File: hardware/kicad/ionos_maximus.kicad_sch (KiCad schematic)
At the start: 45 parts, among them J1 CLH-115-F-D-DV, J2 NA(TC2030-NL), P200 TFC-120-02-F-D-A-K-TR, P201 TFC-120-02-F-D-A-K-TR, U1 LP5907MFX-3.3, U2 CAT24C32WI-GT3

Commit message: Docs from the twin: BRD4265B has no BOARD_ID SDA/SCL pull-ups (Pi 1k8 serve I2C1); P200-37 is USB_VBUS, not 5V
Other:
- note added: "pull-ups: 1k8 on the Pi, none on the radio board (only WP)."
- note removed: "pull-ups 1k8 on the Pi, 10k on the radio board."
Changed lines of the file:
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@@
 		)
 	)
-	(text "pull-ups 1k8 on the Pi, 10k on the radio board."
+	(text "pull-ups: 1k8 on the Pi, none on the radio board (only WP)."
 		(exclude_from_sim no)
 		(at 284.48 121.92 0)
@@
 			)
 		)
-		(property "Description" "P200-37 5 V option, not fitted"
+		(property "Description" "P200-37 = USB_VBUS on BRD4265B (5V is P200-35), not fitted"
 			(at 210.82 182.88 0)
 			(hide yes)

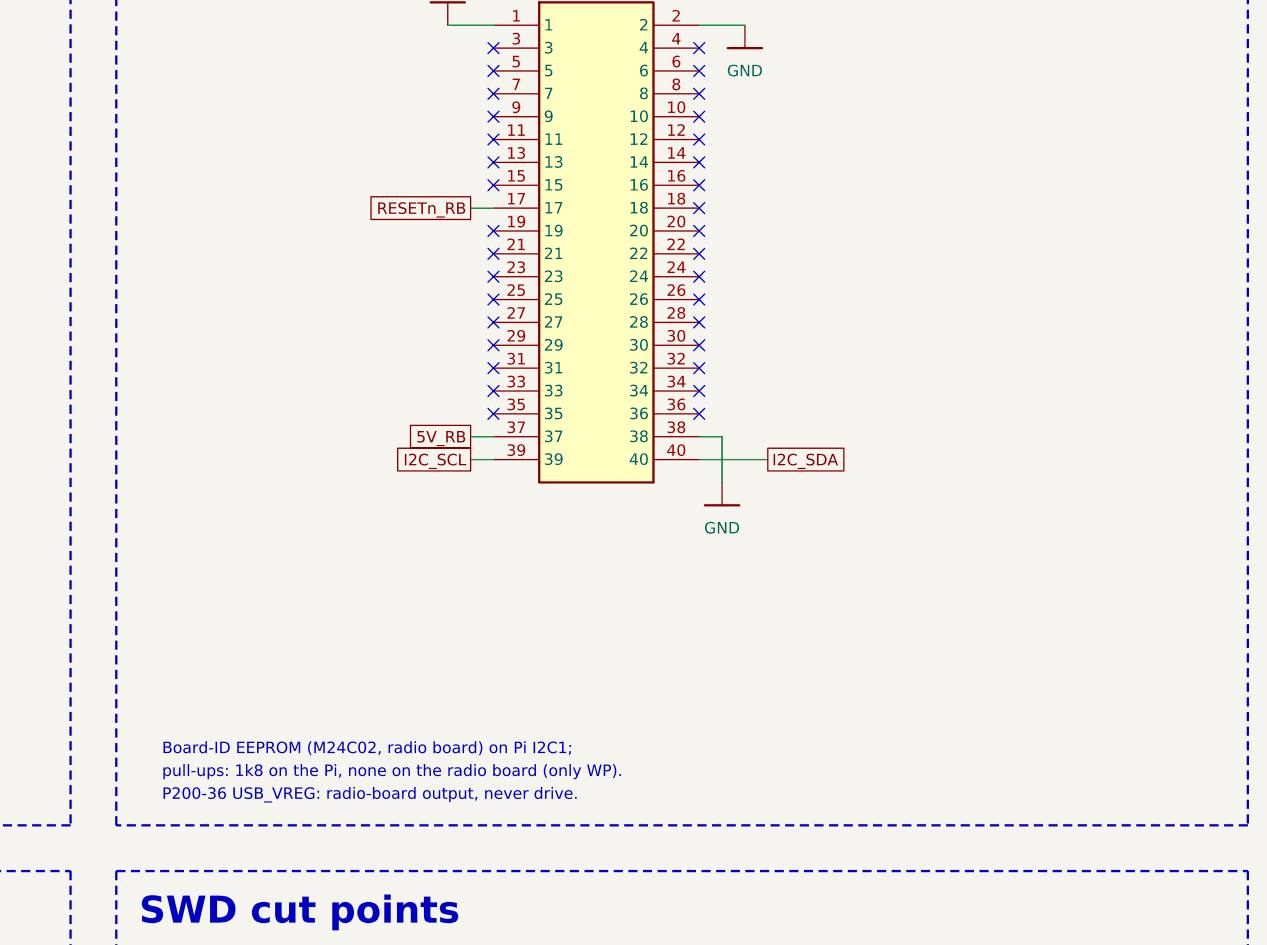
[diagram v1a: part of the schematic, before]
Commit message: P200 board-ID I2C as on ionos-sdr-mini: JP9/JP10 cut points, R18/R19 4.7k pull-ups (DNP, the Pi has 1k8)
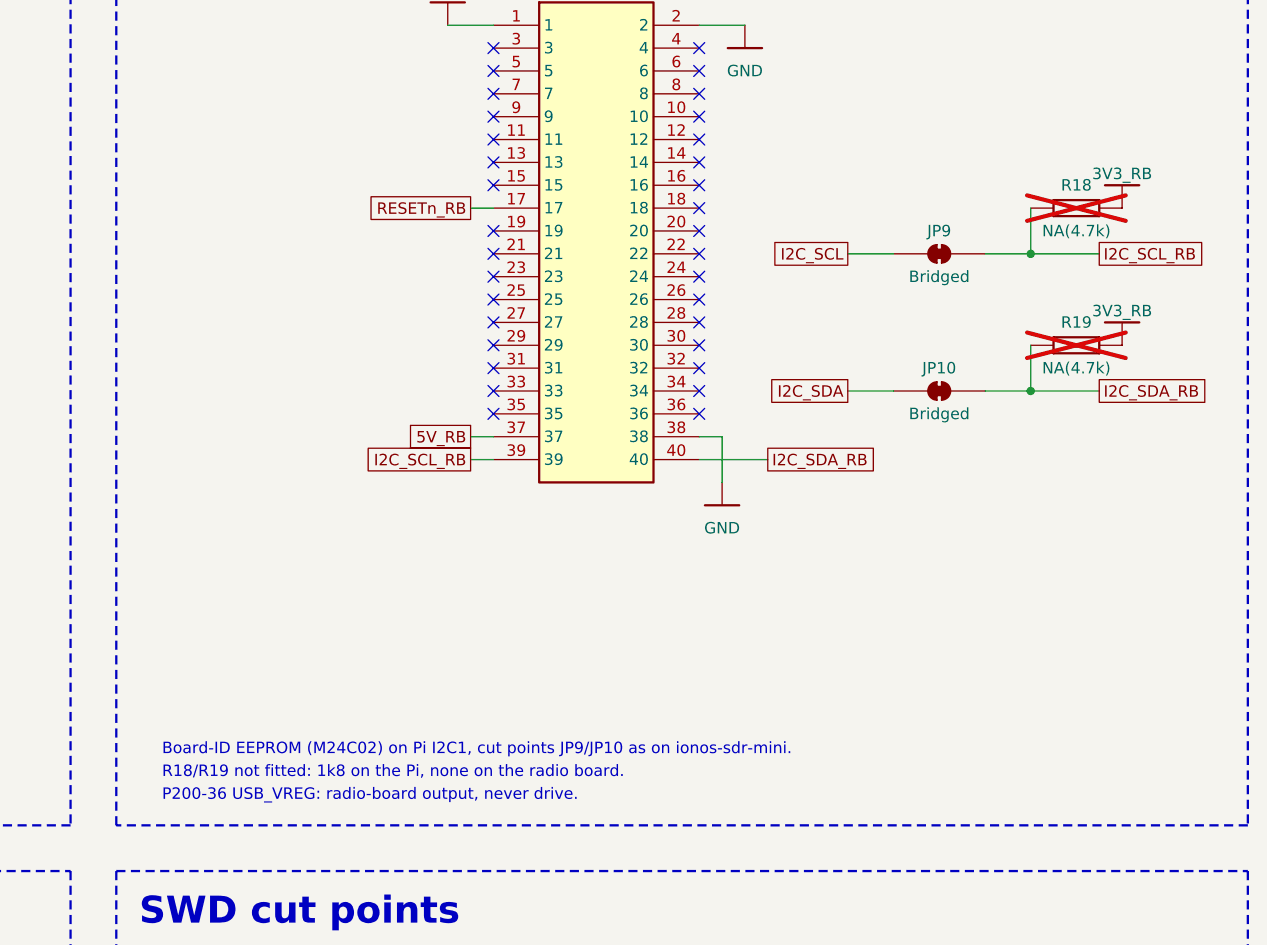
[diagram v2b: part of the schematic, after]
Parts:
- added JP10, JP9: Bridged, Jumper:SolderJumper-2_P1.3mm_Bridged_RoundedPad1.0x1.5mm, symbol ionos_maximus:SJ_Bridged
- added R18, R19: NA(4.7k), ionos_maximus:RESC1005X40_0402, symbol ionos_maximus:R
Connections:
- net 3V3_RB: now also R18.2, R19.2
- net I2C_SCL: now also JP9.1 (A); no longer P200.39
- net I2C_SDA: now also JP10.1 (A); no longer P200.40
- new net I2C_SCL_RB: JP9.2 (B), P200.39, R18.1
- new net I2C_SDA_RB: JP10.2 (B), P200.40, R19.1
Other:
- note added: "Board-ID EEPROM (M24C02) on Pi I2C1, cut points JP9/JP10 as on ionos-sdr-mini."
- note added: "R18/R19 not fitted: 1k8 on the Pi, none on the radio board."
- note removed: "Board-ID EEPROM (M24C02, radio board) on Pi I2C1;"
- note removed: "pull-ups: 1k8 on the Pi, none on the radio board (only WP)."
